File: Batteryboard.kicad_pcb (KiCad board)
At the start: 2 copper layers, 128.9 x 70.5 mm, 76 parts, among them J1 Conn_01x02_Male, J2 Conn_01x03_Male, J3 Conn_01x02_Male, J4 Conn_01x02_Male, Q1 SI7617DN-T1-GE3, Q2 SI7617DN-T1-GE3, Q3 SI7617DN-T1-GE3, Q4 SIS412DN-T1-GE3, Q5 SIS412DN-T1-GE3, Q6 SIS412DN-T1-GE3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

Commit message: fixed an error with D1 footprint
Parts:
- D1: footprint Diode_SMD:D_0805_2012Metric -> Diode_SMD:D_SOD-323
- moved D1 1.63 mm to (117.1, 129.8)
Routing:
- net REGN: track 99.0 -> 100.5 mm
- net BTST: track 93.8 -> 92.8 mm
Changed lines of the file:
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@@
     (thickness 1.6)
     (drawings 6)
-    (tracks 1233)
+    (tracks 1237)
     (zones 0)
     (modules 76)
@@
     (add_net VFB)
   )
+  (module Diode_SMD:D_SOD-323 (layer F.Cu)
+    (at 117.1448 129.794 180)
+    (descr SOD-323)
+    (tags SOD-323)
+    (attr smd)
+    (fp_text reference D1 (at 0 -1.85) (layer F.SilkS)
+      (effects (font (size 1 1) (thickness 0.15)))
+    )
+    (fp_text value D_Schottky (at 0.1 1.9) (layer F.Fab)
+      (effects (font (size 1 1) (thickness 0.15)))
+    )
+    (fp_line (start -1.5 -0.85) (end 1.05 -0.85) (layer F.SilkS) (width 0.12))
+    (fp_line (start -1.5 0.85) (end 1.05 0.85) (layer F.SilkS) (width 0.12))
+    (fp_line (start -1.6 -0.95) (end -1.6 0.95) (layer F.CrtYd) (width 0.05))
+    (fp_line (start -1.6 0.95) (end 1.6 0.95) (layer F.CrtYd) (width 0.05))
+    (fp_line (start 1.6 -0.95) (end 1.6 0.95) (layer F.CrtYd) (width 0.05))
+    (fp_line (start -1.6 -0.95) (end 1.6 -0.95) (layer F.CrtYd) (width 0.05))
+    (fp_line (start -0.9 -0.7) (end 0.9 -0.7) (layer F.Fab) (width 0.1))
+    (fp_line (start 0.9 -0.7) (end 0.9 0.7) (layer F.Fab) (width 0.1))
+    (fp_line (start 0.9 0.7) (end -0.9 0.7) (layer F.Fab) (width 0.1))
+    (fp_line (start -0.9 0.7) (end -0.9 -0.7) (layer F.Fab) (width 0.1))
+    (fp_line (start -0.3 -0.35) (end -0.3 0.35) (layer F.Fab) (width 0.1))
+    (fp_line (start -0.3 0) (end -0.5 0) (layer F.Fab) (width 0.1))
+    (fp_line (start -0.3 0) (end 0.2 -0.35) (layer F.Fab) (width 0.1))
+    (fp_line (start 0.2 -0.35) (end 0.2 0.35) (layer F.Fab) (width 0.1))
+    (fp_line (start 0.2 0.35) (end -0.3 0) (layer F.Fab) (width 0.1))
+    (fp_line (start 0.2 0) (end 0.45 0) (layer F.Fab) (width 0.1))
+    (fp_line (start -1.5 -0.85) (end -1.5 0.85) (layer F.SilkS) (width 0.12))
+    (fp_text user %R (at 0 -1.85) (layer F.Fab)
+      (effects (font (size 1 1) (thickness 0.15)))
+    )
+    (pad 2 smd rect (at 1.05 0 180) (size 0.6 0.45) (layers F.Cu F.Paste F.Mask)
+      (net 4 REGN))
+    (pad 1 smd rect (at -1.05 0 180) (size 0.6 0.45) (layers F.Cu F.Paste F.Mask)
+      (net 5 BTST))
+    (model ${KISYS3DMOD}/Diode_SMD.3dshapes/D_SOD-323.wrl
+      (at (xyz 0 0 0))
+      (scale (xyz 1 1 1))
+      (rotate (xyz 0 0 0))
+    )
+  )
   (module Connector_JST:JST_EH_B3B-EH-A_1x03_P2.50mm_Vertical (layer F.Cu)
     (at 163.9462 140.3858)
@@
     )
   )
-  (module Diode_SMD:D_0805_2012Metric (layer F.Cu)
-    (at 115.8748 128.778 180)
-    (descr "Diode SMD 0805 (2012 Metric), square (rectangular) end terminal, IPC_7351 nominal, (Body size source: https://docs.google.com/spreadsheets/d/1BsfQQcO9C6DZCsRaXUlFlo91Tg2WpOkGARC1WS5S8t0/edit?usp=sharing), generated with kicad-footprint-generator")
-    (tags diode)
-    (attr smd)
-    (fp_text reference D1 (at -0.1252 -2.222) (layer F.SilkS)
-      (effects (font (size 1 1) (thickness 0.15)))
-    )
-    (fp_text value D_Schottky (at 0 1.65) (layer Cmts.User) hide
-      (effects (font (size 1 1) (thickness 0.15)))
-    )
-    (fp_text user %R (at 0 0) (layer F.Fab)
-      (effects (font (size 0.5 0.5) (thickness 0.08)))
-    )
-    (fp_line (start 1.68 0.95) (end -1.68 0.95) (layer F.CrtYd) (width 0.05))
-    (fp_line (start 1.68 -0.95) (end 1.68 0.95) (layer F.CrtYd) (width 0.05))
-    (fp_line (start -1.68 -0.95) (end 1.68 -0.95) (layer F.CrtYd) (width 0.05))
-    (fp_line (start -1.68 0.95) (end -1.68 -0.95) (layer F.CrtYd) (width 0.05))
-    (fp_line (start -1.685 0.96) (end 1 0.96) (layer F.SilkS) (width 0.12))
-    (fp_line (start -1.685 -0.96) (end -1.685 0.96) (layer F.SilkS) (width 0.12))
-    (fp_line (start 1 -0.96) (end -1.685 -0.96) (layer F.SilkS) (width 0.12))
-    (fp_line (start 1 0.6) (end 1 -0.6) (layer F.Fab) (width 0.1))
-    (fp_line (start -1 0.6) (end 1 0.6) (layer F.Fab) (width 0.1))
-    (fp_line (start -1 -0.3) (end -1 0.6) (layer F.Fab) (width 0.1))
-    (fp_line (start -0.7 -0.6) (end -1 -0.3) (layer F.Fab) (width 0.1))
-    (fp_line (start 1 -0.6) (end -0.7 -0.6) (layer F.Fab) (width 0.1))
-    (pad 2 smd roundrect (at 0.9375 0 180) (size 0.975 1.4) (layers F.Cu F.Paste F.Mask) (roundrect_rratio 0.25)
-      (net 4 REGN))
-    (pad 1 smd roundrect (at -0.9375 0 180) (size 0.975 1.4) (layers F.Cu F.Paste F.Mask) (roundrect_rratio 0.25)
-      (net 5 BTST))
-    (model ${KISYS3DMOD}/Diode_SMD.3dshapes/D_0805_2012Metric.wrl
-      (at (xyz 0 0 0))
-      (scale (xyz 1 1 1))
-      (rotate (xyz 0 0 0))
-    )
-  )
   (module Capacitor_SMD:C_0603_1608Metric (layer F.Cu)
     (at 166.624 107.1372)
@@
   (segment (start 119.4308 118.618) (end 120.056201 117.992599) (width 0.762) (layer F.Cu) (net 3))
   (segment (start 120.056201 117.992599) (end 120.056201 115.818483) (width 0.762) (layer F.Cu) (net 3))
-  (segment (start 100.7109 122.7236) (end 100.7109 122.1486) (width 0.762) (layer F.Cu) (net 4))
-  (segment (start 100.7109 127.215288) (end 100.7109 122.7236) (width 0.762) (layer F.Cu) (net 4))
-  (segment (start 103.554622 130.05901) (end 100.7109 127.215288) (width 0.762) (layer F.Cu) (net 4))
-  (segment (start 113.65629 130.05901) (end 103.554622 130.05901) (width 0.762) (layer F.Cu) (net 4))
-  (segment (start 114.9373 128.778) (end 113.65629 130.05901) (width 0.762) (layer F.Cu) (net 4))
-  (segment (start 114.9373 128.778) (end 116.9185 126.7968) (width 0.762) (layer F.Cu) (net 4))
   (segment (start 116.9185 126.7968) (end 117.602 126.7968) (width 0.762) (layer F.Cu) (net 4))
   (segment (start 117.602 126.7968) (end 117.602 126.7968) (width 0.762) (layer F.Cu) (net 4))
@@
   (segment (start 122.694825 103.2002) (end 122.694825 103.221343) (width 0.3556) (layer F.Cu) (net 4))
   (segment (start 122.694825 103.221343) (end 122.2632 103.652968) (width 0.3556) (layer F.Cu) (net 4))
+  (segment (start 113.65629 130.05901) (end 113.9213 129.794) (width 0.762) (layer F.Cu) (net 4))
+  (segment (start 103.554622 130.05901) (end 113.65629 130.05901) (width 0.762) (layer F.Cu) (net 4))
+  (segment (start 100.7109 122.1486) (end 100.7109 127.215288) (width 0.762) (layer F.Cu) (net 4))
+  (segment (start 100.7109 127.215288) (end 103.554622 130.05901) (width 0.762) (layer F.Cu) (net 4))
+  (segment (start 115.4684 128.2469) (end 116.9185 126.7968) (width 0.762) (layer F.Cu) (net 4))
+  (segment (start 115.4684 129.794) (end 115.4684 128.2469) (width 0.762) (layer F.Cu) (net 4))
+  (segment (start 115.4684 129.794) (end 116.0948 129.794) (width 0.762) (layer F.Cu) (net 4))
+  (segment (start 113.9213 129.794) (end 115.4684 129.794) (width 0.762) (layer F.Cu) (net 4))
   (segment (start 132.1054 122.428) (end 132.1054 127.941514) (width 0.762) (layer F.Cu) (net 5))
   (segment (start 131.547724 128.49919) (end 124.23081 128.49919) (width 0.762) (layer F.Cu) (net 5))
-  (segment (start 123.952 128.778) (end 116.8123 128.778) (width 0.762) (layer F.Cu) (net 5))
   (segment (start 124.23081 128.49919) (end 123.952 128.778) (width 0.762) (layer F.Cu) (net 5))
   (segment (start 137.568289 120.29759) (end 140.763608 120.29759) (width 0.762) (layer F.Cu) (net 5))
@@
   (segment (start 132.715 92.71) (end 127.3048 92.71) (width 0.762) (layer F.Cu) (net 5))
   (segment (start 131.547724 128.49919) (end 132.1054 127.941514) (width 0.762) (layer F.Cu) (net 5))
+  (segment (start 121.128518 128.778) (end 123.952 128.778) (width 0.762) (layer F.Cu) (net 5))
+  (segment (start 120.112518 129.794) (end 121.128518 128.778) (width 0.762) (layer F.Cu) (net 5))
+  (segment (start 118.1948 129.794) (end 120.112518 129.794) (width 0.762) (layer F.Cu) (net 5))
   (segment (start 87.4776 104.0107) (end 86.24739 105.24091) (width 0.762) (layer F.Cu) (net 6))
   (segment (start 97.7392 98.3996) (end 97.7392 98.3996) (width 0.762) (layer F.Cu) (net 6))

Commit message: final touches before stefka, fixed a couple small things
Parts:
- L1: footprint Inductor_SMD:L_0603_1608Metric -> Inductor_SMD:L_Vishay_IHLP-2525
- R10/RT1, R9, R9/RT2: footprint Resistor_SMD:R_0805_2012Metric -> Resistor_SMD:R_0603_1608Metric
- moved L1 45.8 mm to (93.9, 89.2)
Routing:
- net SRP: track 36.6 -> 90.1 mm, vias 0 -> 4
- net Q4S: track 63.2 -> 103.7 mm, vias 4 -> 5
- net Net-(NTCTH1/NTCG163JF103FT1S1-Pad2): track 19.4 -> 22.0 mm
- net Net-(C4-Pad1): track 90.8 -> 93.2 mm
- net Net-(R9-Pad1): track 5.42 -> 6.84 mm
- net Net-(Q9-Pad4): track 22.0 -> 23.2 mm
- net Q5S: track 122.3 -> 123.3 mm
- net Q5G: track 35.8 -> 34.9 mm

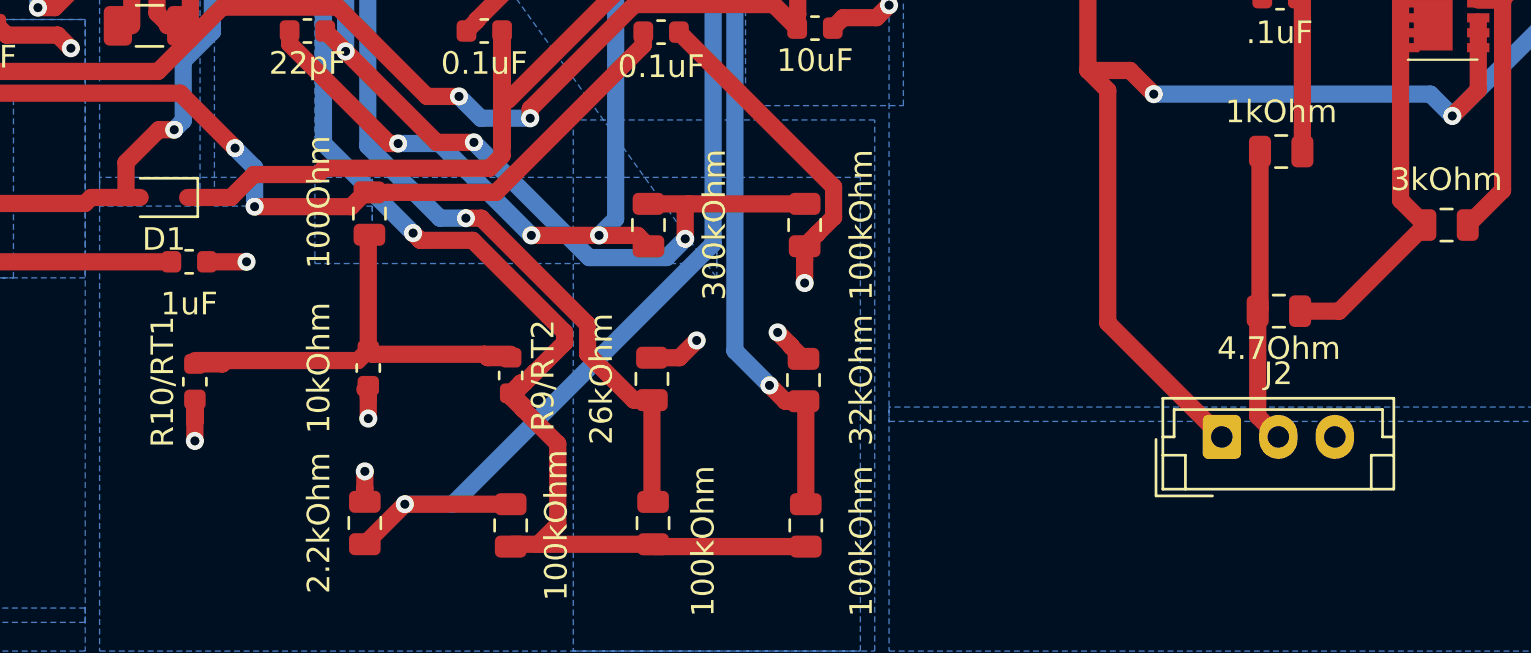
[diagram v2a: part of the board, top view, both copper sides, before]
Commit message: fixed J2, wrong footprint
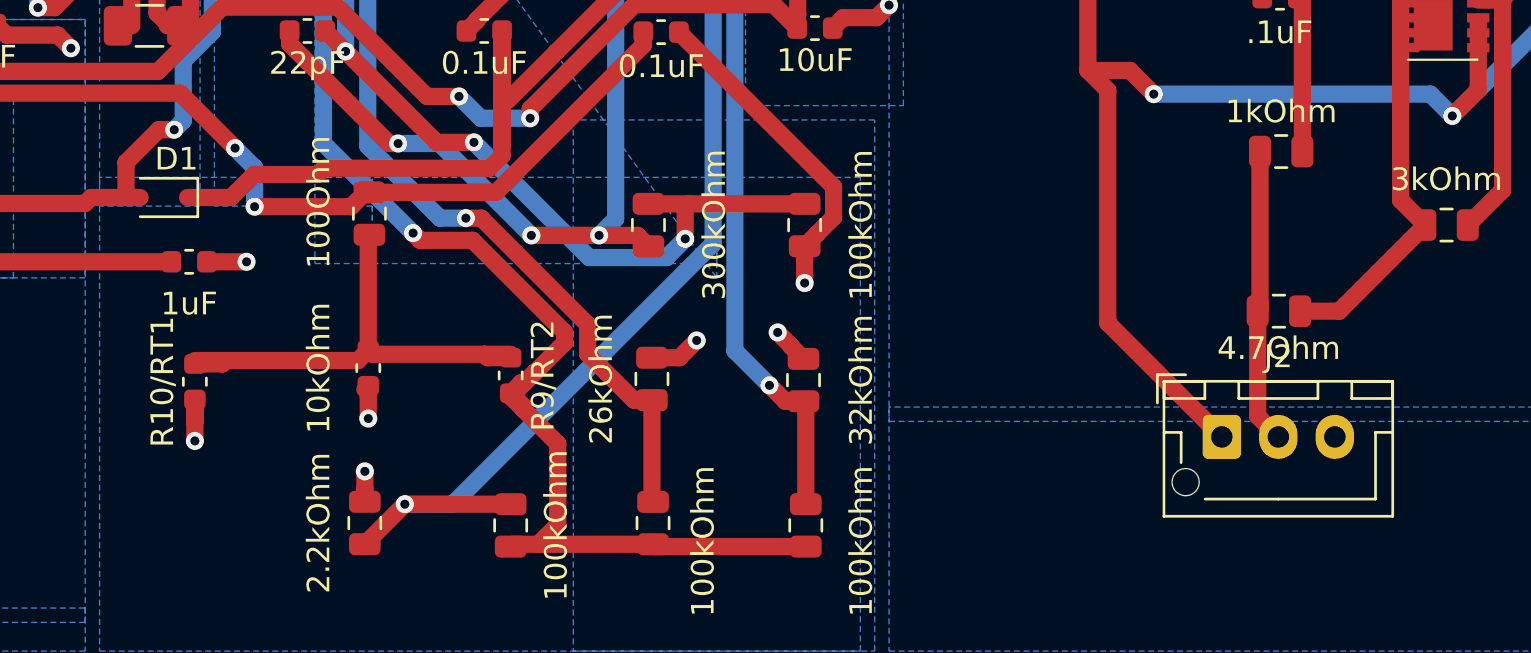
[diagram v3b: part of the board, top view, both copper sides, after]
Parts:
- J2: footprint Connector_JST:JST_EH_B3B-EH-A_1x03_P2.50mm_Vertical -> Connector_JST:JST_XH_B3B-XH-AM_1x03_P2.50mm_Vertical
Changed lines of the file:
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@@
   )
   (setup
-    (last_trace_width 0.762)
+    (last_trace_width 0.25)
     (user_trace_width 0.2794)
     (user_trace_width 0.3048)
@@
     (pcbplotparams
       (layerselection 0x010fc_ffffffff)
-      (usegerberextensions false)
+      (usegerberextensions true)
       (usegerberattributes false)
       (usegerberadvancedattributes false)
-      (creategerberjobfile false)
+      (creategerberjobfile true)
       (excludeedgelayer true)
       (linewidth 0.100000)
@@
       (outputformat 1)
       (mirror false)
-      (drillshape 1)
+      (drillshape 0)
       (scaleselection 1)
-      (outputdirectory ""))
+      (outputdirectory "../"))
   )
   (net 0 "")
@@
     (add_net VFB)
   )
+  (module Connector_JST:JST_XH_B3B-XH-AM_1x03_P2.50mm_Vertical (layer F.Cu)
+    (at 163.9462 140.3858)
+    (descr "JST XH series connector, B3B-XH-AM, with boss (http://www.jst-mfg.com/product/pdf/eng/eXH.pdf), generated with kicad-footprint-generator")
+    (tags "connector JST XH vertical boss")
+    (fp_text reference J2 (at 2.5 -3.55) (layer F.SilkS)
+      (effects (font (size 1 1) (thickness 0.15)))
+    )
+    (fp_text value Conn_01x03_Male (at 2.5 4.6) (layer F.Fab)
+      (effects (font (size 1 1) (thickness 0.15)))
+    )
+    (fp_text user %R (at 2.5 2.7) (layer F.Fab)
+      (effects (font (size 1 1) (thickness 0.15)))
+    )
+    (fp_line (start -2.85 -2.75) (end -2.85 -1.5) (layer F.SilkS) (width 0.12))
+    (fp_line (start -1.6 -2.75) (end -2.85 -2.75) (layer F.SilkS) (width 0.12))
+    (fp_line (start 6.8 2.75) (end 2.5 2.75) (layer F.SilkS) (width 0.12))
+    (fp_line (start 6.8 -0.2) (end 6.8 2.75) (layer F.SilkS) (width 0.12))
+    (fp_line (start 7.55 -0.2) (end 6.8 -0.2) (layer F.SilkS) (width 0.12))
+    (fp_line (start 2.5 2.75) (end -0.74 2.75) (layer F.SilkS) (width 0.12))
+    (fp_line (start -1.8 -0.2) (end -1.8 1.14) (layer F.SilkS) (width 0.12))
+    (fp_line (start -2.55 -0.2) (end -1.8 -0.2) (layer F.SilkS) (width 0.12))
+    (fp_line (start 7.55 -2.45) (end 5.75 -2.45) (layer F.SilkS) (width 0.12))
+    (fp_line (start 7.55 -1.7) (end 7.55 -2.45) (layer F.SilkS) (width 0.12))
+    (fp_line (start 5.75 -1.7) (end 7.55 -1.7) (layer F.SilkS) (width 0.12))
+    (fp_line (start 5.75 -2.45) (end 5.75 -1.7) (layer F.SilkS) (width 0.12))
+    (fp_line (start -0.75 -2.45) (end -2.55 -2.45) (layer F.SilkS) (width 0.12))
+    (fp_line (start -0.75 -1.7) (end -0.75 -2.45) (layer F.SilkS) (width 0.12))
+    (fp_line (start -2.55 -1.7) (end -0.75 -1.7) (layer F.SilkS) (width 0.12))
+    (fp_line (start -2.55 -2.45) (end -2.55 -1.7) (layer F.SilkS) (width 0.12))
+    (fp_line (start 4.25 -2.45) (end 0.75 -2.45) (layer F.SilkS) (width 0.12))
+    (fp_line (start 4.25 -1.7) (end 4.25 -2.45) (layer F.SilkS) (width 0.12))
+    (fp_line (start 0.75 -1.7) (end 4.25 -1.7) (layer F.SilkS) (width 0.12))
+    (fp_line (start 0.75 -2.45) (end 0.75 -1.7) (layer F.SilkS) (width 0.12))
+    (fp_line (start 0 -1.35) (end 0.625 -2.35) (layer F.Fab) (width 0.1))
+    (fp_line (start -0.625 -2.35) (end 0 -1.35) (layer F.Fab) (width 0.1))
+    (fp_line (start 7.95 -2.85) (end -2.95 -2.85) (layer F.CrtYd) (width 0.05))
+    (fp_line (start 7.95 3.9) (end 7.95 -2.85) (layer F.CrtYd) (width 0.05))
+    (fp_line (start -2.95 3.9) (end 7.95 3.9) (layer F.CrtYd) (width 0.05))
+    (fp_line (start -2.95 -2.85) (end -2.95 3.9) (layer F.CrtYd) (width 0.05))
+    (fp_line (start 7.56 -2.46) (end -2.56 -2.46) (layer F.SilkS) (width 0.12))
+    (fp_line (start 7.56 3.51) (end 7.56 -2.46) (layer F.SilkS) (width 0.12))
+    (fp_line (start -2.56 3.51) (end 7.56 3.51) (layer F.SilkS) (width 0.12))
+    (fp_line (start -2.56 -2.46) (end -2.56 3.51) (layer F.SilkS) (width 0.12))
+    (fp_line (start 7.45 -2.35) (end -2.45 -2.35) (layer F.Fab) (width 0.1))
+    (fp_line (start 7.45 3.4) (end 7.45 -2.35) (layer F.Fab) (width 0.1))
+    (fp_line (start -2.45 3.4) (end 7.45 3.4) (layer F.Fab) (width 0.1))
+    (fp_line (start -2.45 -2.35) (end -2.45 3.4) (layer F.Fab) (width 0.1))
+    (pad "" np_thru_hole circle (at -1.6 2) (size 1.2 1.2) (drill 1.2) (layers *.Cu *.Mask))
+    (pad 3 thru_hole oval (at 5 0) (size 1.7 1.95) (drill 0.95) (layers *.Cu *.Mask)
+      (net 34 Q5S))
+    (pad 2 thru_hole oval (at 2.5 0) (size 1.7 1.95) (drill 0.95) (layers *.Cu *.Mask)
+      (net 26 "Net-(J2-Pad2)"))
+    (pad 1 thru_hole roundrect (at 0 0) (size 1.7 1.95) (drill 0.95) (layers *.Cu *.Mask) (roundrect_rratio 0.147059)
+      (net 37 Q6S))
+    (model ${KISYS3DMOD}/Connector_JST.3dshapes/JST_XH_B3B-XH-AM_1x03_P2.50mm_Vertical.wrl
+      (at (xyz 0 0 0))
+      (scale (xyz 1 1 1))
+      (rotate (xyz 0 0 0))
+    )
+  )
   (module Resistor_SMD:R_0603_1608Metric (layer F.Cu)
     (at 132.4864 137.668 270)
@@
       (effects (font (size 1 1) (thickness 0.15)))
     )
-    (fp_text value 6.8uH (at 0 4.675) (layer F.Fab)
+    (fp_text value 6.8uH (at 7.112 1.6256) (layer F.Fab)
       (effects (font (size 1 1) (thickness 0.15)))
     )
@@
     (fp_line (start -3.175 3.175) (end 3.175 3.175) (layer F.Fab) (width 0.1))
     (fp_line (start -3.175 -3.175) (end -3.175 3.175) (layer F.Fab) (width 0.1))
-    (fp_text user %R (at -1.3209 0.4318) (layer F.Fab)
+    (fp_text user %R (at 6.2738 3.6576) (layer F.Fab)
       (effects (font (size 1 1) (thickness 0.15)))
     )
@@
     (tags SOD-323)
     (attr smd)
-    (fp_text reference D1 (at 0 -1.85) (layer F.SilkS)
-      (effects (font (size 1 1) (thickness 0.15)))
-    )
-    (fp_text value D_Schottky (at 0.1 1.9) (layer F.Fab)
+    (fp_text reference D1 (at -0.5588 1.7018) (layer F.SilkS)
+      (effects (font (size 1 1) (thickness 0.15)))
+    )
+    (fp_text value D_Schottky (at -0.4064 -1.3208) (layer F.Fab) hide
       (effects (font (size 1 1) (thickness 0.15)))
     )
@@
     (fp_line (start 0.2 0) (end 0.45 0) (layer F.Fab) (width 0.1))
     (fp_line (start -1.5 -0.85) (end -1.5 0.85) (layer F.SilkS) (width 0.12))
-    (fp_text user %R (at 0 -1.85) (layer F.Fab)
+    (fp_text user %R (at 3.1242 1.3208) (layer F.Fab) hide
       (effects (font (size 1 1) (thickness 0.15)))
     )
@@
       (at (xyz 0 0 0))
       (scale (xyz 1 1 1))
-      (rotate (xyz 0 0 0))
-    )
-  )
-  (module Connector_JST:JST_EH_B3B-EH-A_1x03_P2.50mm_Vertical (layer F.Cu)
-    (at 163.9462 140.3858)
-    (descr "JST EH series connector, B3B-EH-A (http://www.jst-mfg.com/product/pdf/eng/eEH.pdf), generated with kicad-footprint-generator")
-    (tags "connector JST EH vertical")
-    (fp_text reference J2 (at 2.5 -2.8) (layer F.SilkS)
-      (effects (font (size 1 1) (thickness 0.15)))
-    )
-    (fp_text value Conn_01x03_Male (at 2.5 3.4) (layer F.Fab)
-      (effects (font (size 1 1) (thickness 0.15)))
-    )
-    (fp_text user %R (at 2.5 1.5) (layer F.Fab)
-      (effects (font (size 1 1) (thickness 0.15)))
-    )
-    (fp_line (start -2.91 2.61) (end -0.41 2.61) (layer F.Fab) (width 0.1))
-    (fp_line (start -2.91 0.11) (end -2.91 2.61) (layer F.Fab) (width 0.1))
-    (fp_line (start -2.91 2.61) (end -0.41 2.61) (layer F.SilkS) (width 0.12))
-    (fp_line (start -2.91 0.11) (end -2.91 2.61) (layer F.SilkS) (width 0.12))
-    (fp_line (start 6.61 0.81) (end 6.61 2.31) (layer F.SilkS) (width 0.12))
-    (fp_line (start 7.61 0.81) (end 6.61 0.81) (layer F.SilkS) (width 0.12))
-    (fp_line (start -1.61 0.81) (end -1.61 2.31) (layer F.SilkS) (width 0.12))
-    (fp_line (start -2.61 0.81) (end -1.61 0.81) (layer F.SilkS) (width 0.12))
-    (fp_line (start 7.11 0) (end 7.61 0) (layer F.SilkS) (width 0.12))
-    (fp_line (start 7.11 -1.21) (end 7.11 0) (layer F.SilkS) (width 0.12))
-    (fp_line (start -2.11 -1.21) (end 7.11 -1.21) (layer F.SilkS) (width 0.12))
-    (fp_line (start -2.11 0) (end -2.11 -1.21) (layer F.SilkS) (width 0.12))
-    (fp_line (start -2.61 0) (end -2.11 0) (layer F.SilkS) (width 0.12))
-    (fp_line (start 7.61 -1.71) (end -2.61 -1.71) (layer F.SilkS) (width 0.12))
-    (fp_line (start 7.61 2.31) (end 7.61 -1.71) (layer F.SilkS) (width 0.12))
-    (fp_line (start -2.61 2.31) (end 7.61 2.31) (layer F.SilkS) (width 0.12))
-    (fp_line (start -2.61 -1.71) (end -2.61 2.31) (layer F.SilkS) (width 0.12))
-    (fp_line (start 8 -2.1) (end -3 -2.1) (layer F.CrtYd) (width 0.05))
-    (fp_line (start 8 2.7) (end 8 -2.1) (layer F.CrtYd) (width 0.05))
-    (fp_line (start -3 2.7) (end 8 2.7) (layer F.CrtYd) (width 0.05))
-    (fp_line (start -3 -2.1) (end -3 2.7) (layer F.CrtYd) (width 0.05))
-    (fp_line (start 7.5 -1.6) (end -2.5 -1.6) (layer F.Fab) (width 0.1))
-    (fp_line (start 7.5 2.2) (end 7.5 -1.6) (layer F.Fab) (width 0.1))
-    (fp_line (start -2.5 2.2) (end 7.5 2.2) (layer F.Fab) (width 0.1))
-    (fp_line (start -2.5 -1.6) (end -2.5 2.2) (layer F.Fab) (width 0.1))
-    (pad 3 thru_hole oval (at 5 0) (size 1.7 1.95) (drill 0.95) (layers *.Cu *.Mask)
-      (net 34 Q5S))
-    (pad 2 thru_hole oval (at 2.5 0) (size 1.7 1.95) (drill 0.95) (layers *.Cu *.Mask)
-      (net 26 "Net-(J2-Pad2)"))
-    (pad 1 thru_hole roundrect (at 0 0) (size 1.7 1.95) (drill 0.95) (layers *.Cu *.Mask) (roundrect_rratio 0.147059)
-      (net 37 Q6S))
-    (model ${KISYS3DMOD}/Connector_JST.3dshapes/JST_EH_B3B-EH-A_1x03_P2.50mm_Vertical.wrl
-      (at (xyz 0 0 0))
-      (scale (xyz 1 1 1))
